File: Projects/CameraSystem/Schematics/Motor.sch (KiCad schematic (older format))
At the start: 16 parts, among them J13 Conn_02x02_Odd_Even

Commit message: camera was updated
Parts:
- removed D?: LED, LED_SMD:LED_1206_3216Metric, symbol Device:LED
- removed Q?: BC856, Package_TO_SOT_SMD:SOT-23, symbol Transistor_BJT:BC856
- removed R? (x2): 10k, symbol Device:R
- removed R?: 560, digikey-footprints:0603, symbol Device:R
- added D10: RED_LED, LED_SMD:LED_1206_3216Metric, symbol Device:LED
- added Q3, Q4: BC847, Package_TO_SOT_SMD:SOT-23, symbol Transistor_BJT:BC847
- added R34, R36: 47k, Resistor_SMD:R_0603_1608Metric_Pad1.05x0.95mm_HandSolder, symbol Device:R
- added R37: 560, Resistor_SMD:R_0603_1608Metric_Pad1.05x0.95mm_HandSolder, symbol Device:R
- C24, C25, C26: renamed from C?; footprint (none) -> Capacitor_SMD:C_0603_1608Metric_Pad1.05x0.95mm_HandSolder
- D9: renamed from D?; value LED -> GREEN_LED
- J10: renamed from J13; footprint Pin_Headers:Pin_Header_Straight_2x02_Pitch2.54mm_SMD -> Connector_PinSocket_2.54mm:PinSocket_2x02_P2.54mm_Vertical
- J11: renamed from J?; footprint (none) -> Connector_PinSocket_2.54mm:PinSocket_2x03_P2.54mm_Vertical
- R31, R32, R33: renamed from R?; footprint (none) -> Resistor_SMD:R_0603_1608Metric_Pad1.05x0.95mm_HandSolder
- R35: renamed from R?; footprint digikey-footprints:0603 -> Resistor_SMD:R_0603_1608Metric_Pad1.05x0.95mm_HandSolder
- gave numbers to parts that had none: 1
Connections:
- wire segments 76 -> 81
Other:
- note removed: "ADD IC drv8833 and switches"
- moved on the sheet: D9, R35

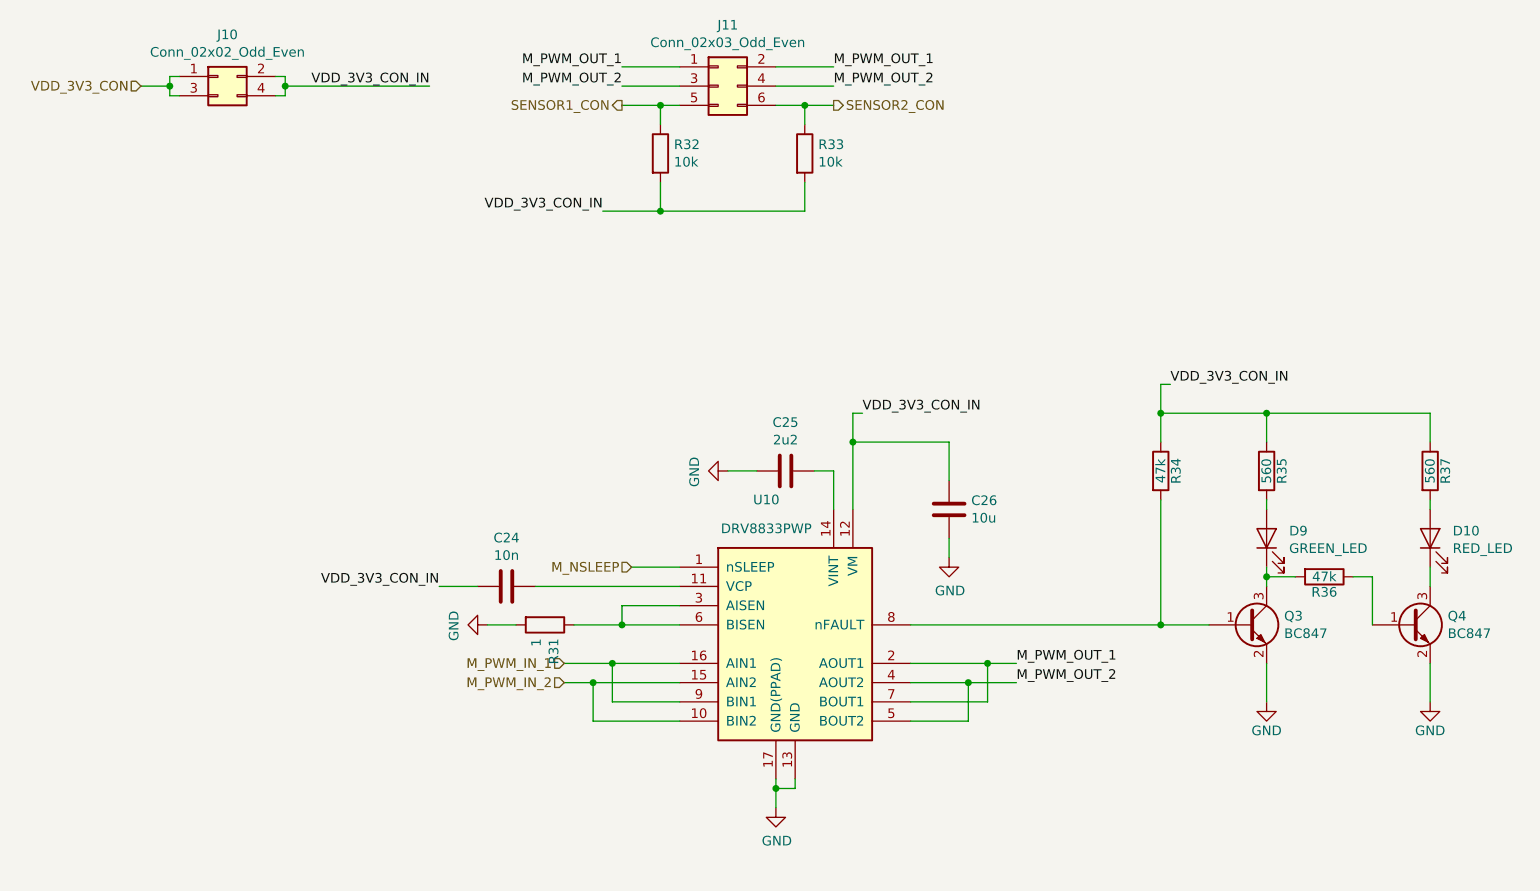
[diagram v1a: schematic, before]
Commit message: camera was updated
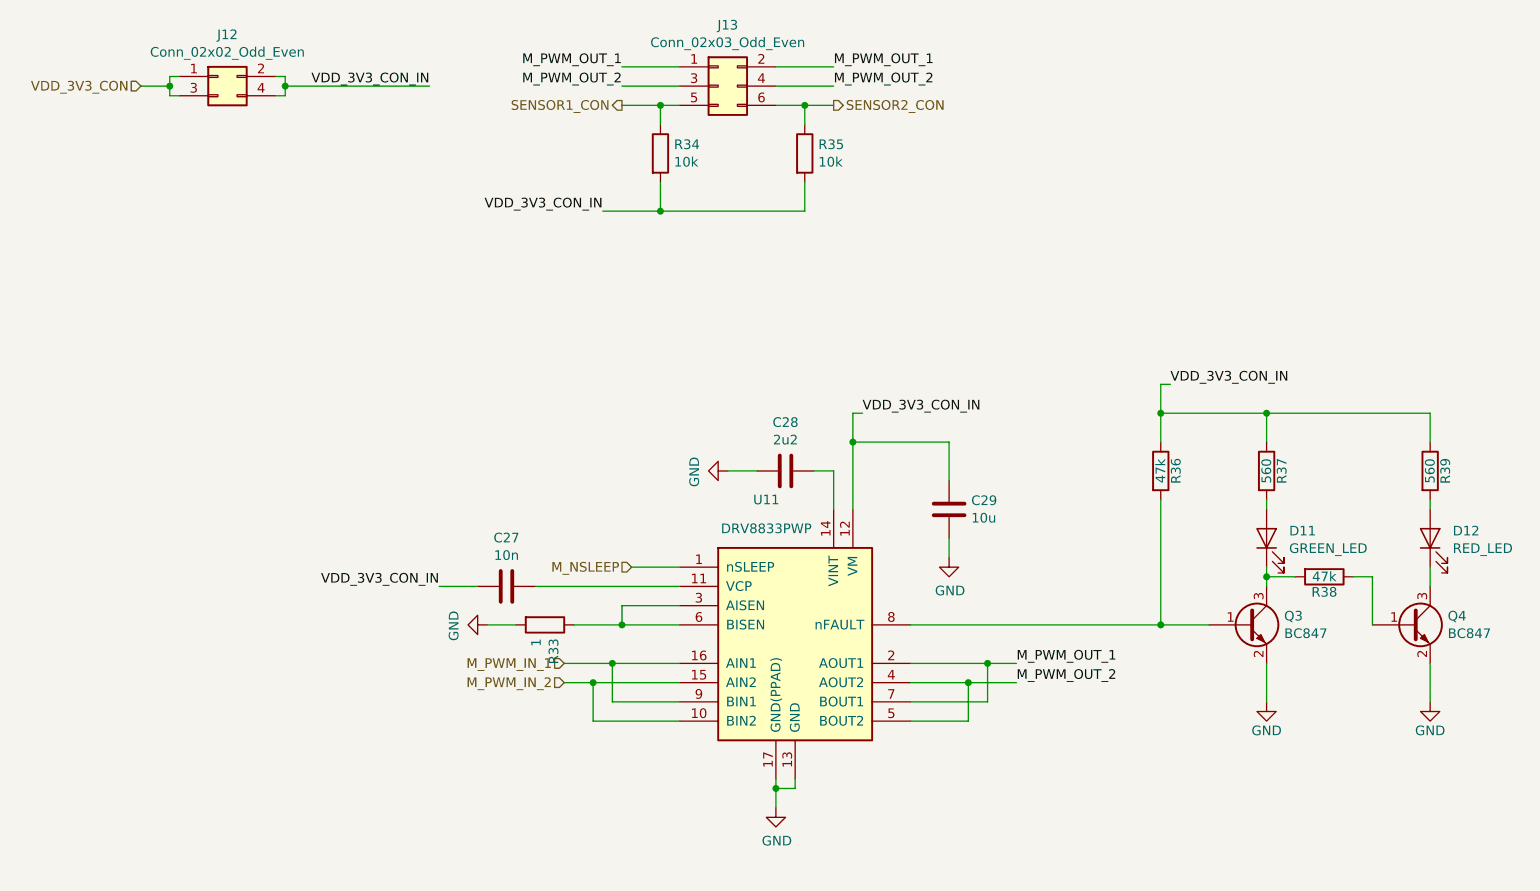
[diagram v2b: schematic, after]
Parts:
- renumbered C24 to C27, C25 to C28, C26 to C29, D9 to D11, D10 to D12, J10 to J12, J11 to J13, R31 to R33, R32 to R34, R33 to R35, R34 to R36, R35 to R37, R36 to R38, R37 to R39, U10 to U11
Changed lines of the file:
@@
 $Descr A4 11693 8268
 encoding utf-8
-Sheet 8 9
+Sheet 9 9
 Title ""
 Date ""
@@
 	1450 1450 1600 1450
 $Comp
-L Connector_Generic:Conn_02x02_Odd_Even J10
+L Connector_Generic:Conn_02x02_Odd_Even J12
 U 1 1 5BC62F82
 P 1850 1400
-F 0 "J10" H 1900 1617 50  0000 C CNN
+F 0 "J12" H 1900 1617 50  0000 C CNN
 F 1 "Conn_02x02_Odd_Even" H 1900 1526 50  0000 C CNN
 F 2 "Connector_PinSocket_2.54mm:PinSocket_2x02_P2.54mm_Vertical" H 1850 1400 50  0001 C CNN
@@
 	2200 1500 2200 1450
 $Comp
-L Driver_Motor:DRV8833PWP U10
+L Driver_Motor:DRV8833PWP U11
 U 1 1 5CA61180
 P 4850 4350
-F 0 "U10" H 4700 5100 50  0000 C CNN
+F 0 "U11" H 4700 5100 50  0000 C CNN
 F 1 "DRV8833PWP" H 4700 4950 50  0000 C CNN
 F 2 "Package_SO:HTSSOP-16-1EP_4.4x5mm_P0.65mm_EP3.4x5mm_Mask2.46x2.31mm_ThermalVias" H 5300 4800 50  0001 L CNN
@@
 M_PWM_IN_2
 $Comp
-L power:GND #PWR038
+L power:GND #PWR049
 U 1 1 5CA6CB5D
 P 4750 5200
-F 0 "#PWR038" H 4750 4950 50  0001 C CNN
+F 0 "#PWR049" H 4750 4950 50  0001 C CNN
 F 1 "GND" H 4755 5027 50  0000 C CNN
 F 2 "" H 4750 5200 50  0001 C CNN
@@
 Connection ~ 5850 4450
 $Comp
-L Device:C C26
+L Device:C C29
 U 1 1 5CA72244
 P 5650 3650
-F 0 "C26" H 5765 3696 50  0000 L CNN
+F 0 "C29" H 5765 3696 50  0000 L CNN
 F 1 "10u" H 5765 3605 50  0000 L CNN
 F 2 "Capacitor_SMD:C_0603_1608Metric_Pad1.05x0.95mm_HandSolder" H 5688 3500 50  0001 C CNN
@@
 $EndComp
 $Comp
-L power:GND #PWR039
+L power:GND #PWR050
 U 1 1 5CA7228E
 P 5650 3900
-F 0 "#PWR039" H 5650 3650 50  0001 C CNN
+F 0 "#PWR050" H 5650 3650 50  0001 C CNN
 F 1 "GND" H 5655 3727 50  0000 C CNN
 F 2 "" H 5650 3900 50  0001 C CNN
@@
 Connection ~ 5150 3300
 $Comp
-L Device:C C24
+L Device:C C27
 U 1 1 5CA74C23
 P 3350 4050
-F 0 "C24" V 3098 4050 50  0000 C CNN
+F 0 "C27" V 3098 4050 50  0000 C CNN
 F 1 "10n" V 3189 4050 50  0000 C CNN
 F 2 "Capacitor_SMD:C_0603_1608Metric_Pad1.05x0.95mm_HandSolder" H 3388 3900 50  0001 C CNN
@@
 $EndComp
 $Comp
-L Device:C C25
+L Device:C C28
 U 1 1 5CA752A9
 P 4800 3450
-F 0 "C25" V 5052 3450 50  0000 C CNN
+F 0 "C28" V 5052 3450 50  0000 C CNN
 F 1 "2u2" V 4961 3450 50  0000 C CNN
 F 2 "Capacitor_SMD:C_0603_1608Metric_Pad1.05x0.95mm_HandSolder" H 4838 3300 50  0001 C CNN
@@
 $EndComp
 $Comp
-L power:GND #PWR037
+L power:GND #PWR048
 U 1 1 5CA75356
 P 4500 3450
-F 0 "#PWR037" H 4500 3200 50  0001 C CNN
+F 0 "#PWR048" H 4500 3200 50  0001 C CNN
 F 1 "GND" H 4505 3277 50  0000 C CNN
 F 2 "" H 4500 3450 50  0001 C CNN
@@
 Connection ~ 3950 4250
 $Comp
-L Device:R R31
+L Device:R R33
 U 1 1 5CA6DD8F
 P 3550 4250
-F 0 "R31" H 3620 4296 50  0000 L CNN
+F 0 "R33" H 3620 4296 50  0000 L CNN
 F 1 "1" H 3620 4205 50  0000 L CNN
 F 2 "Resistor_SMD:R_0603_1608Metric_Pad1.05x0.95mm_HandSolder" V 3480 4250 50  0001 C CNN
@@
 $EndComp
 $Comp
-L power:GND #PWR036
+L power:GND #PWR047
 U 1 1 5CA6DE44
 P 3250 4250
-F 0 "#PWR036" H 3250 4000 50  0001 C CNN
+F 0 "#PWR047" H 3250 4000 50  0001 C CNN
 F 1 "GND" H 3255 4077 50  0000 C CNN
 F 2 "" H 3250 4250 50  0001 C CNN
@@
 M_PWM_OUT_2
 $Comp
-L Connector_Generic:Conn_02x03_Odd_Even J11
+L Connector_Generic:Conn_02x03_Odd_Even J13
 U 1 1 5CA7377C
 P 4450 1450
-F 0 "J11" H 4500 1767 50  0000 C CNN
+F 0 "J13" H 4500 1767 50  0000 C CNN
 F 1 "Conn_02x03_Odd_Even" H 4500 1676 50  0000 C CNN
 F 2 "Connector_PinSocket_2.54mm:PinSocket_2x03_P2.54mm_Vertical" H 4450 1450 50  0001 C CNN
@@
 SENSOR2_CON
 $Comp
-L Device:R R32
+L Device:R R34
 U 1 1 5CA79CEF
 P 4150 1800
-F 0 "R32" H 4220 1846 50  0000 L CNN
+F 0 "R34" H 4220 1846 50  0000 L CNN
 F 1 "10k" H 4220 1755 50  0000 L CNN
 F 2 "Resistor_SMD:R_0603_1608Metric_Pad1.05x0.95mm_HandSolder" V 4080 1800 50  0001 C CNN
@@
 $EndComp
 $Comp
-L Device:R R33
+L Device:R R35
 U 1 1 5CA79D4B
 P 4900 1800
-F 0 "R33" H 4970 1846 50  0000 L CNN
+F 0 "R35" H 4970 1846 50  0000 L CNN
 F 1 "10k" H 4970 1755 50  0000 L CNN
 F 2 "Resistor_SMD:R_0603_1608Metric_Pad1.05x0.95mm_HandSolder" V 4830 1800 50  0001 C CNN
@@
 P 7300 3450
 AR Path="/5BB4C1AE/5CA944BE" Ref="R?"  Part="1"
-AR Path="/5BC611AE/5CA944BE" Ref="R35"  Part="1"
-F 0 "R35" V 7380 3450 50  0000 C CNN
+AR Path="/5BC611AE/5CA944BE" Ref="R37"  Part="1"
+F 0 "R37" V 7380 3450 50  0000 C CNN
 F 1 "560" V 7300 3450 50  0000 C CNN
 F 2 "Resistor_SMD:R_0603_1608Metric_Pad1.05x0.95mm_HandSolder" V 7230 3450 50  0001 C CNN
@@
 	7300 3950 7300 4000
 $Comp
-L Device:LED D9
+L Device:LED D11
 U 1 1 5CA944CE
 P 7300 3800
-F 0 "D9" V 7338 3683 50  0000 R CNN
+F 0 "D11" V 7338 3683 50  0000 R CNN
 F 1 "GREEN_LED" V 7247 3683 50  0000 R CNN
 F 2 "LED_SMD:LED_1206_3216Metric" H 7300 3800 50  0001 C CNN
@@
 P 6750 3450
 AR Path="/5BB4C1AE/5CA9BD8A" Ref="R?"  Part="1"
-AR Path="/5BC611AE/5CA9BD8A" Ref="R34"  Part="1"
-F 0 "R34" V 6830 3450 50  0000 C CNN
+AR Path="/5BC611AE/5CA9BD8A" Ref="R36"  Part="1"
+F 0 "R36" V 6830 3450 50  0000 C CNN
 F 1 "47k" V 6750 3450 50  0000 C CNN
 F 2 "Resistor_SMD:R_0603_1608Metric_Pad1.05x0.95mm_HandSolder" V 6680 3450 50  0001 C CNN
@@
 	7300 4450 7300 4650
 $Comp
-L power:GND #PWR040
+L power:GND #PWR051
 U 1 1 5CAB44B3
 P 7300 4650
-F 0 "#PWR040" H 7300 4400 50  0001 C CNN
+F 0 "#PWR051" H 7300 4400 50  0001 C CNN
 F 1 "GND" H 7300 4500 50  0000 C CNN
 F 2 "" H 7300 4650 50  0001 C CNN
@@
 P 8150 3450
 AR Path="/5BB4C1AE/5CAB79CF" Ref="R?"  Part="1"
-AR Path="/5BC611AE/5CAB79CF" Ref="R37"  Part="1"
-F 0 "R37" V 8230 3450 50  0000 C CNN
+AR Path="/5BC611AE/5CAB79CF" Ref="R39"  Part="1"
+F 0 "R39" V 8230 3450 50  0000 C CNN
 F 1 "560" V 8150 3450 50  0000 C CNN
 F 2 "Resistor_SMD:R_0603_1608Metric_Pad1.05x0.95mm_HandSolder" V 8080 3450 50  0001 C CNN
@@
 	8150 3950 8150 4050
 $Comp
-L Device:LED D10
+L Device:LED D12
 U 1 1 5CAB79D7
 P 8150 3800
-F 0 "D10" V 8188 3683 50  0000 R CNN
+F 0 "D12" V 8188 3683 50  0000 R CNN
 F 1 "RED_LED" V 8097 3683 50  0000 R CNN
 F 2 "LED_SMD:LED_1206_3216Metric" H 8150 3800 50  0001 C CNN
@@
 	8150 4450 8150 4650
 $Comp
-L power:GND #PWR041
+L power:GND #PWR052
 U 1 1 5CAB79E7
 P 8150 4650
-F 0 "#PWR041" H 8150 4400 50  0001 C CNN
+F 0 "#PWR052" H 8150 4400 50  0001 C CNN
 F 1 "GND" H 8150 4500 50  0000 C CNN
 F 2 "" H 8150 4650 50  0001 C CNN
@@
 P 7600 4000
 AR Path="/5BB4C1AE/5CAB92EF" Ref="R?"  Part="1"
-AR Path="/5BC611AE/5CAB92EF" Ref="R36"  Part="1"
-F 0 "R36" V 7680 4000 50  0000 C CNN
+AR Path="/5BC611AE/5CAB92EF" Ref="R38"  Part="1"
+F 0 "R38" V 7680 4000 50  0000 C CNN
 F 1 "47k" V 7600 4000 50  0000 C CNN
 F 2 "Resistor_SMD:R_0603_1608Metric_Pad1.05x0.95mm_HandSolder" V 7530 4000 50  0001 C CNN

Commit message: camera layout updated
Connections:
- net M_PWM_OUT_1: now also J13.3 (Pin_3), J13.4 (Pin_4); no longer J13.1 (Pin_1), J13.2 (Pin_2)
- net M_PWM_OUT_2: now also J13.1 (Pin_1), J13.2 (Pin_2); no longer J13.3 (Pin_3), J13.4 (Pin_4)
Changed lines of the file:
@@
 Wire Wire Line
 	4250 1550 4150 1550
+Text Label 5050 1450 0    50   ~ 0
+M_PWM_OUT_1
+Text Label 3950 1450 2    50   ~ 0
+M_PWM_OUT_1
 Text Label 5050 1350 0    50   ~ 0
-M_PWM_OUT_1
+M_PWM_OUT_2
 Text Label 3950 1350 2    50   ~ 0
-M_PWM_OUT_1
-Text Label 5050 1450 0    50   ~ 0
-M_PWM_OUT_2
-Text Label 3950 1450 2    50   ~ 0
 M_PWM_OUT_2
 Text HLabel 3950 1550 0    50   Output ~ 0
